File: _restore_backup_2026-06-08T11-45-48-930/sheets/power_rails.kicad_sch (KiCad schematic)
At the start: 30 parts, among them J1 0826-1X1T-HS-F, U1 DFLS130LQ-7, U2 DFLS130LQ-7, U3 DFLS130LQ-7, U4 DFLS130LQ-7, U5 TPS2372-4RGWR

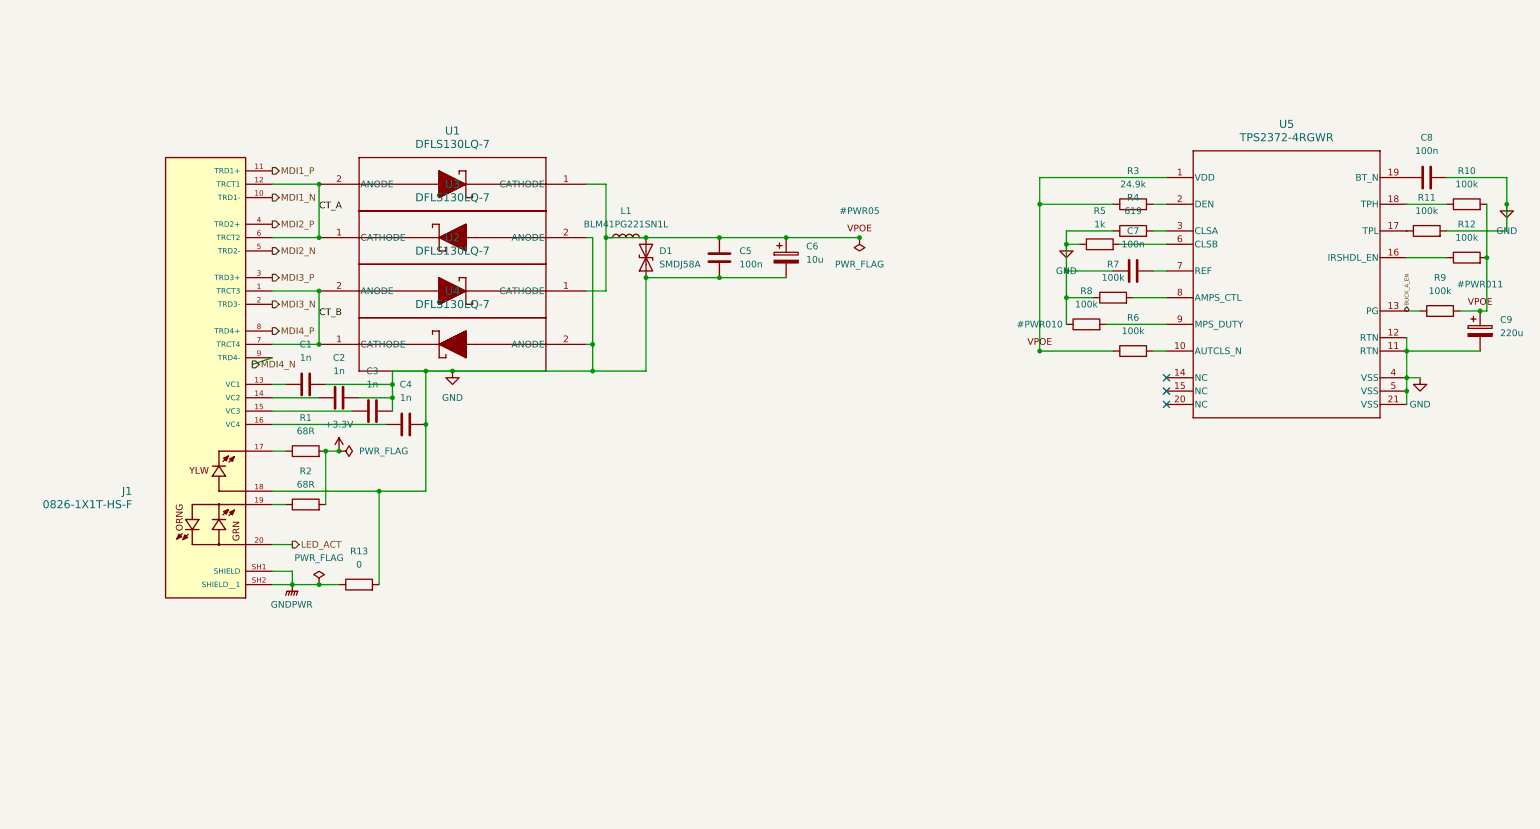
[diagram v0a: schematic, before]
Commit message: Complete Sheet 3 - Power Rails (Buck A and Buck B)
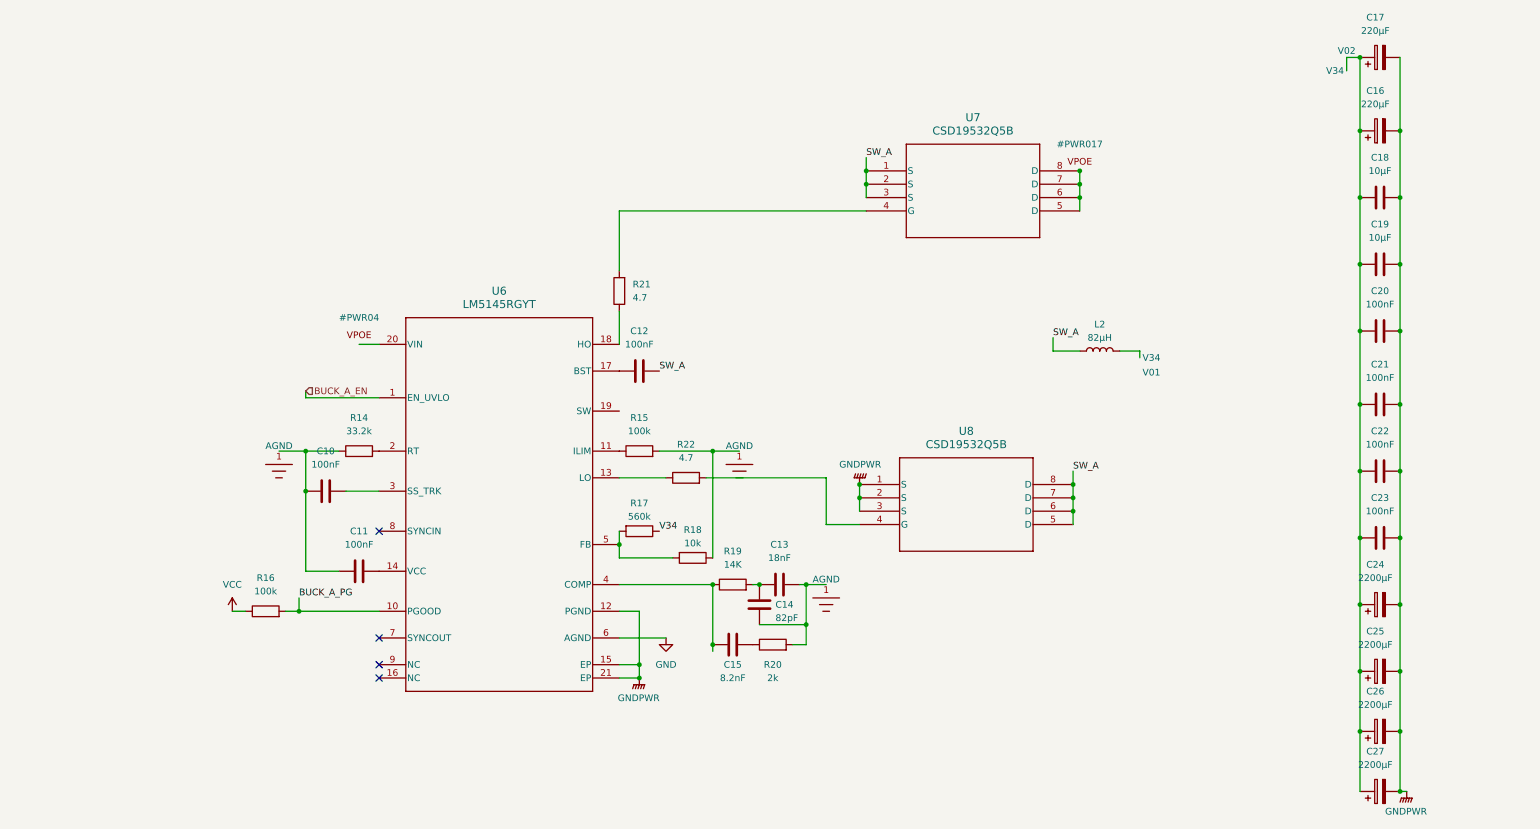
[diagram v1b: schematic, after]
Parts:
- removed C1, C2, C3, C4: 1n, symbol Device:C
- removed C5, C7, C8: 100n, symbol Device:C
- removed C6: 10u, symbol Device:C_Polarized
- removed C9: 220u, symbol Device:C_Polarized
- removed D1: SMDJ58A, symbol Device:D_TVS
- removed J1: 0826-1X1T-HS-F, 0826-1X1T-HS-F:BEL_0826-1X1T-HS-F, symbol poe-aes67-amp:0826-1X1T-HS-F
- removed L1: BLM41PG221SN1L, symbol Device:L
- removed R1, R2: 68R, symbol Device:R
- removed R10, R11, R12, R6, R7, R8, R9: 100k, symbol Device:R
- removed R13: 0, symbol Device:R
- removed R3: 24.9k, symbol Device:R
- removed R4: 619, symbol Device:R
- removed R5: 1k, symbol Device:R
- removed U1, U2, U3, U4: DFLS130LQ-7, DFLS130-7_DIO, symbol poe-aes67-amp:DFLS130LQ-7
- removed U5: TPS2372-4RGWR, RGW0020B, symbol poe-aes67-amp:TPS2372-4RGWR
- added C10, C11, C12, C20, C21, C22, C23: 100nF, symbol Device:C
- added C13: 18nF, symbol Device:C
- added C14: 82pF, symbol Device:C
- added C15: 8.2nF, symbol Device:C
- added C16, C17: 220µF, symbol Device:C_Polarized
- added C18, C19: 10µF, symbol Device:C
- added C24, C25, C26, C27: 2200µF, symbol Device:C_Polarized
- added L2: 82µH, symbol Device:L
- added R14: 33.2k, symbol Device:R
- added R15, R16: 100k, symbol Device:R
- added R17: 560k, symbol Device:R
- added R18: 10k, symbol Device:R
- added R19: 14K, symbol Device:R
- added R20: 2k, symbol Device:R
- added R21, R22: 4.7, symbol Device:R
- added U6: LM5145RGYT, RGY0020B, symbol poe-aes67-amp:LM5145RGYT
- added U7, U8: CSD19532Q5B, DNK8, symbol poe-aes67-amp:CSD19532Q5B
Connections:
- net BUCK_A_EN: now also U6.1 (EN_UVLO)
- net GND: now also U6.6 (AGND)
- net GNDPWR: now also C16.2, C17.2, C18.2, C19.2, C20.2, C21.2, C22.2, C23.2, C24.2, C25.2, C26.2, C27.2, U6.12 (PGND), U6.15 (EP), U6.21 (EP), U8.1 (S), U8.2 (S), U8.3 (S)
- new net: C16.1, C17.1, C18.1, C19.1, C20.1, C21.1, C22.1, C23.1, C24.1, C25.1, C26.1, C27.1
- new net: C13.1, C14.1, R19.2
- new net: C13.2, C14.2, R20.2
- new net: C10.1, C11.1, R14.1
- new net: C10.2, U6.3 (SS_TRK)
- new net: R21.1, U6.18 (HO)
- new net: R21.2, U7.4 (G)
- new net: C15.1, R19.1, U6.4 (COMP)
- new net: C15.2, R20.1
- new net: C12.1, U6.17 (BST)
- new net: C11.2, U6.14 (VCC)
- new net: R22.2, U8.4 (G)
- new net: R15.2, R18.1
- new net: R17.2, R18.2, U6.5 (FB)
- new net: R14.2, U6.2 (RT)
- new net: U7.5 (D), U7.6 (D), U7.7 (D), U7.8 (D)
- new net: R15.1, U6.11 (ILIM)
- new net: R22.1, U6.13 (LO)
- new net BUCK_A_PG: R16.2, U6.10 (PGOOD)
- new net SW_A: C12.2, L2.1, U7.1 (S), U7.2 (S), U7.3 (S), U8.5 (D), U8.6 (D), U8.7 (D), U8.8 (D)
- new net V34: R17.1
- new net VCC: R16.1
- no-connect marks 3 -> 4
